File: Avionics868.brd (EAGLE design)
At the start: 88.8 x 22.9 mm, 65 parts, among them SW1 SPST_TACT-KMR2, U1 ATSAMD21G18_QFN, U2 SPX3819M5-L-3-0, U3 MCP73831T-2ACI/OT, U4 MPU-9250, U5 SIM868, U6 BMP180, X1 JSTPH, X2 32.768, X3 microUSB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

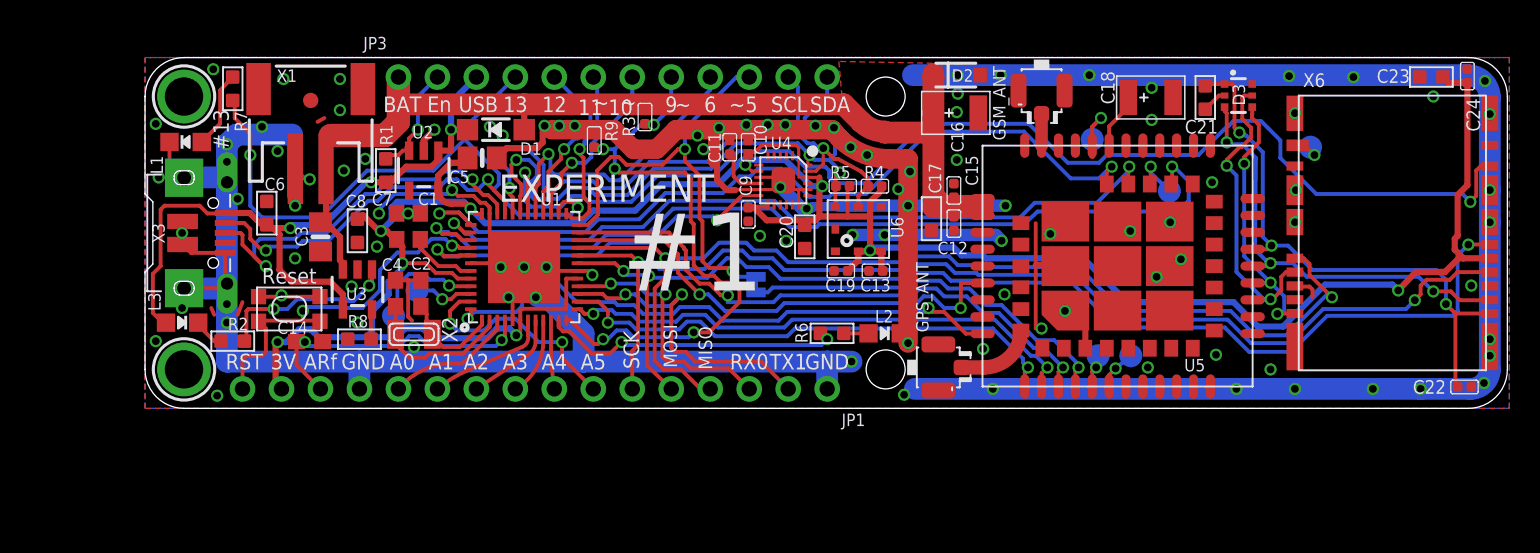
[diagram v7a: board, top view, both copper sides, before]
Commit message: Changed LEDs to Seeed ++
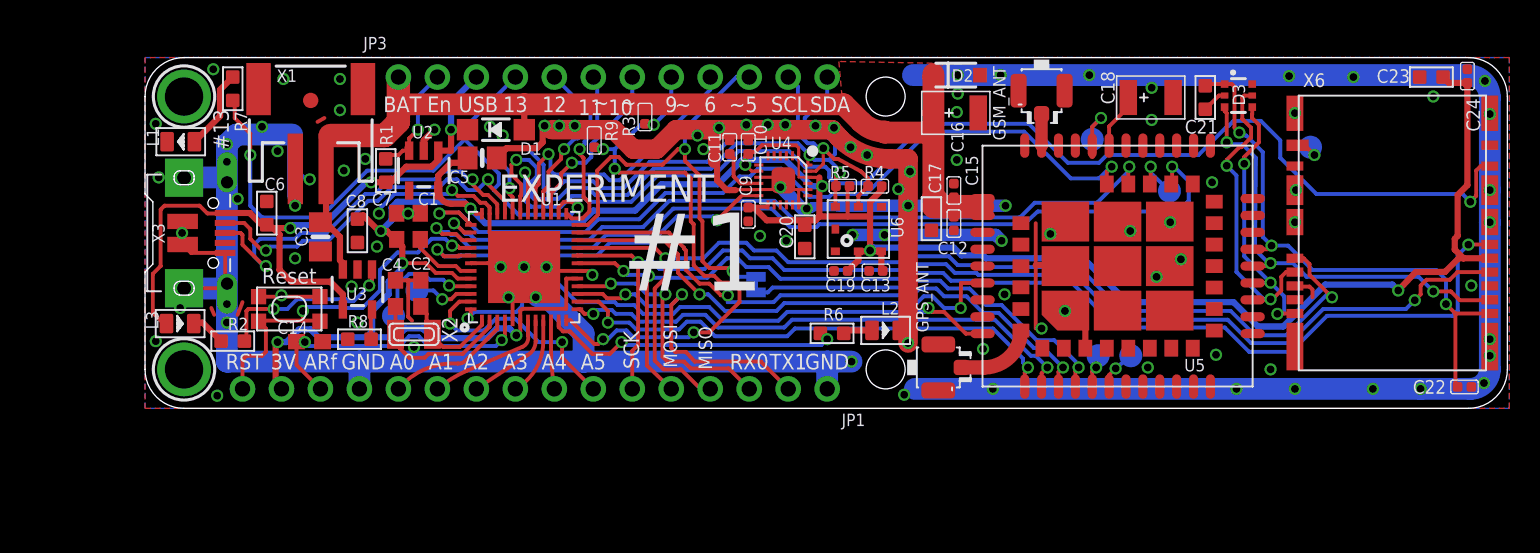
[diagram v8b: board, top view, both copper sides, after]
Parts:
- L1: value RED -> RED-0805; device microbuilder:CHIPLED_0805_NOOUTLINE -> Seeed-LED-2016:LED-0805
- L2: value GREEN -> GREEN-0805; device microbuilder:CHIPLED_0805_NOOUTLINE -> Seeed-LED-2016:LED-0805
- L3: value BLUE -> CLEAR-BLUE-0805; device microbuilder:CHIPLED_0805_NOOUTLINE -> Seeed-LED-2016:LED-0805
- moved L1 0.32 mm to (2.33, 17.4), turned to 180 degrees
- moved L2 0.20 mm to (48.3, 5.08), turned to 0 degrees
- moved L3 0.14 mm to (2.29, 5.52), turned to 0 degrees
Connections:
- net GND: now also L1.-, L2.-; no longer L1.C, L2.C
- net N$1: now also L3.-; no longer L3.C
- net N$2: now also L2.+, R6.2; no longer L1.A, R7.2
- net N$8: now also L1.+, R7.2; no longer L2.A, R6.2
- net VBUS: now also L3.+; no longer L3.A
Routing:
- net N$8: track 1.62 -> 5.25 mm
- net N$2: track 5.06 -> 1.92 mm
- net GND: track 319.6 -> 317.2 mm
